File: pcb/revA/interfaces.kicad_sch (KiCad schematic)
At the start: 18 parts, among them J2 Conn_02x30_Row_Letter_First, SW1 SW_DIP_x05, U22 SN74LV1T34DBV, U3 74AHCT1G125DB, U4 SN74CB3T3245PW, U5 SN74CB3T3245PW, U6 SN74CB3T3245PW, U7 SN74CB3T3245PW

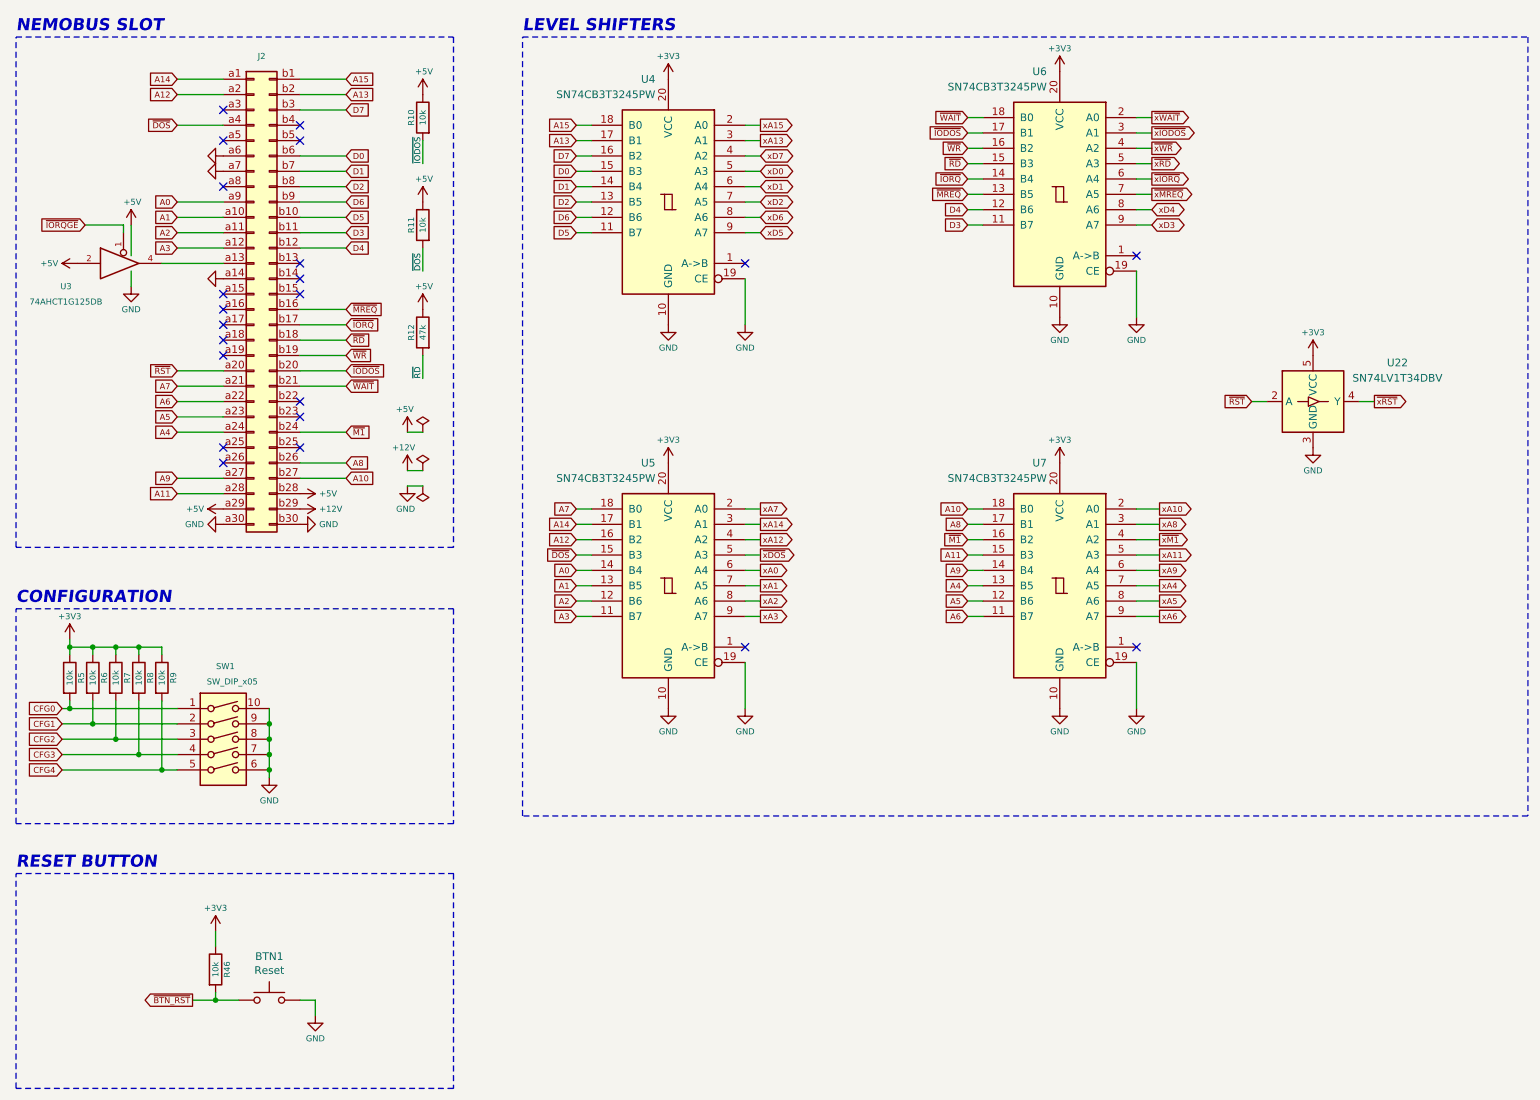
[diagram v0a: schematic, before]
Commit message: Updated gerbers to min 0.2/0.45 vias, firmware build for xc6slx16
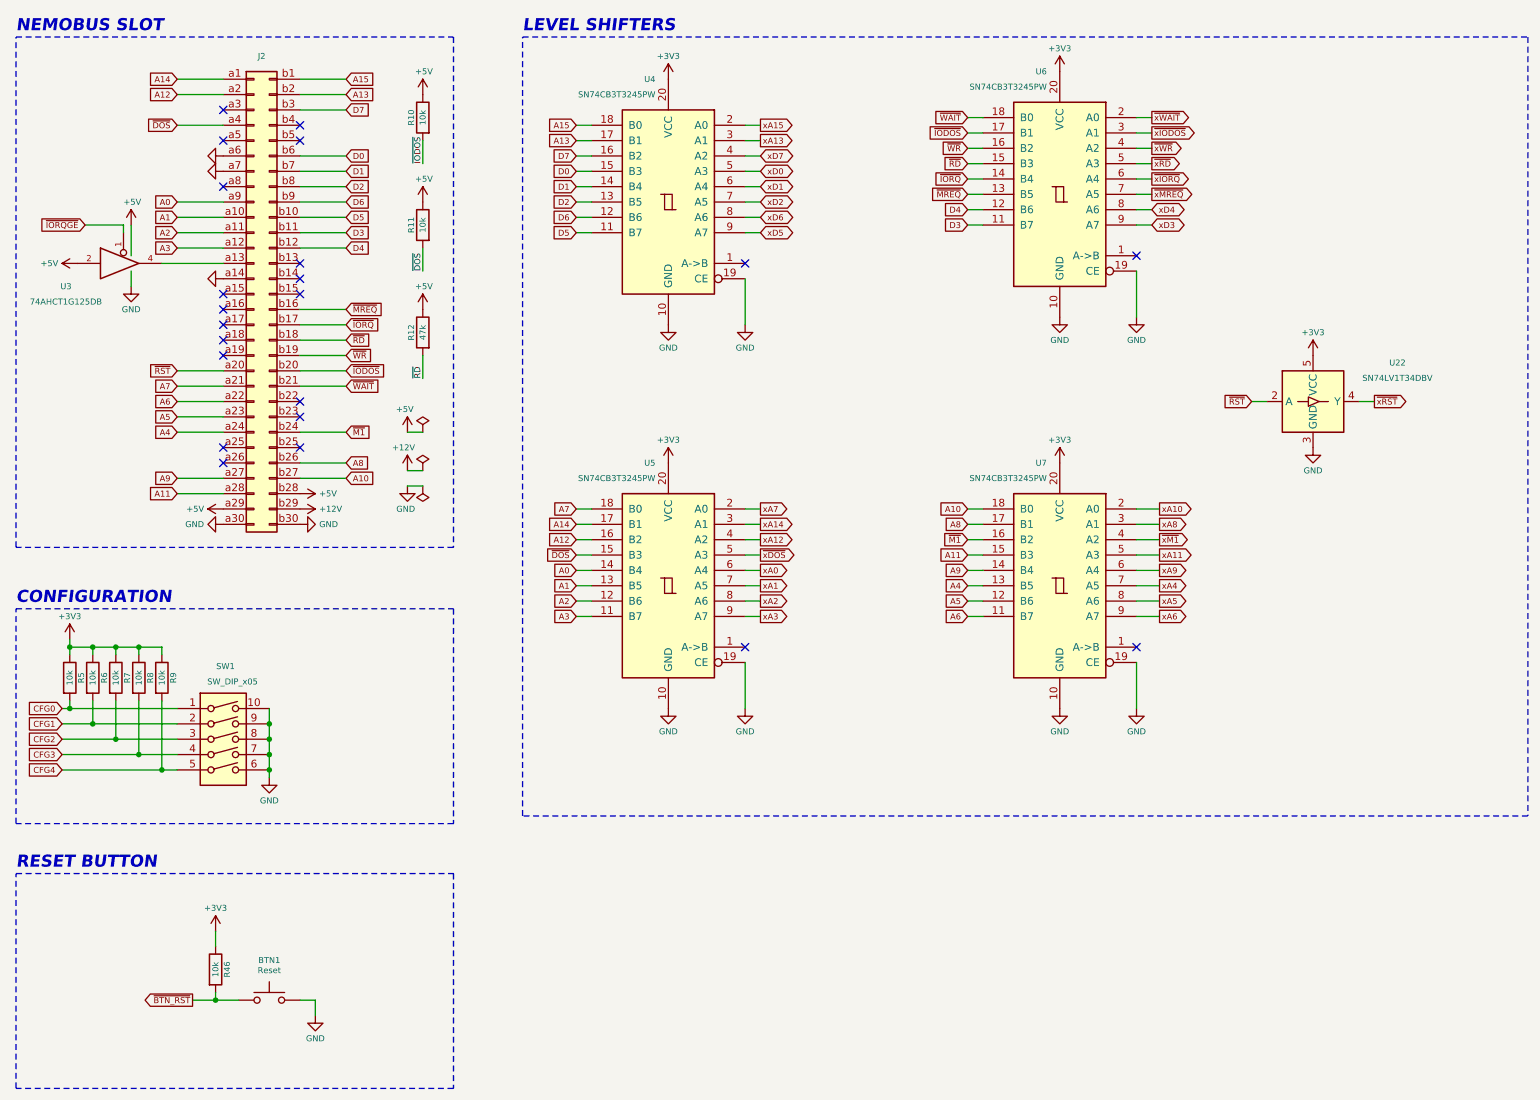
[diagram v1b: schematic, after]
